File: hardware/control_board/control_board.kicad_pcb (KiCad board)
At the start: 4 copper layers, 70 x 50 mm, 9 parts, among them J1 USB-C, J2 USB-C, J3 TX24-60R-6ST-H1E, J4 TX24-60R-6ST-H1E, U1 STUSB4500QTR

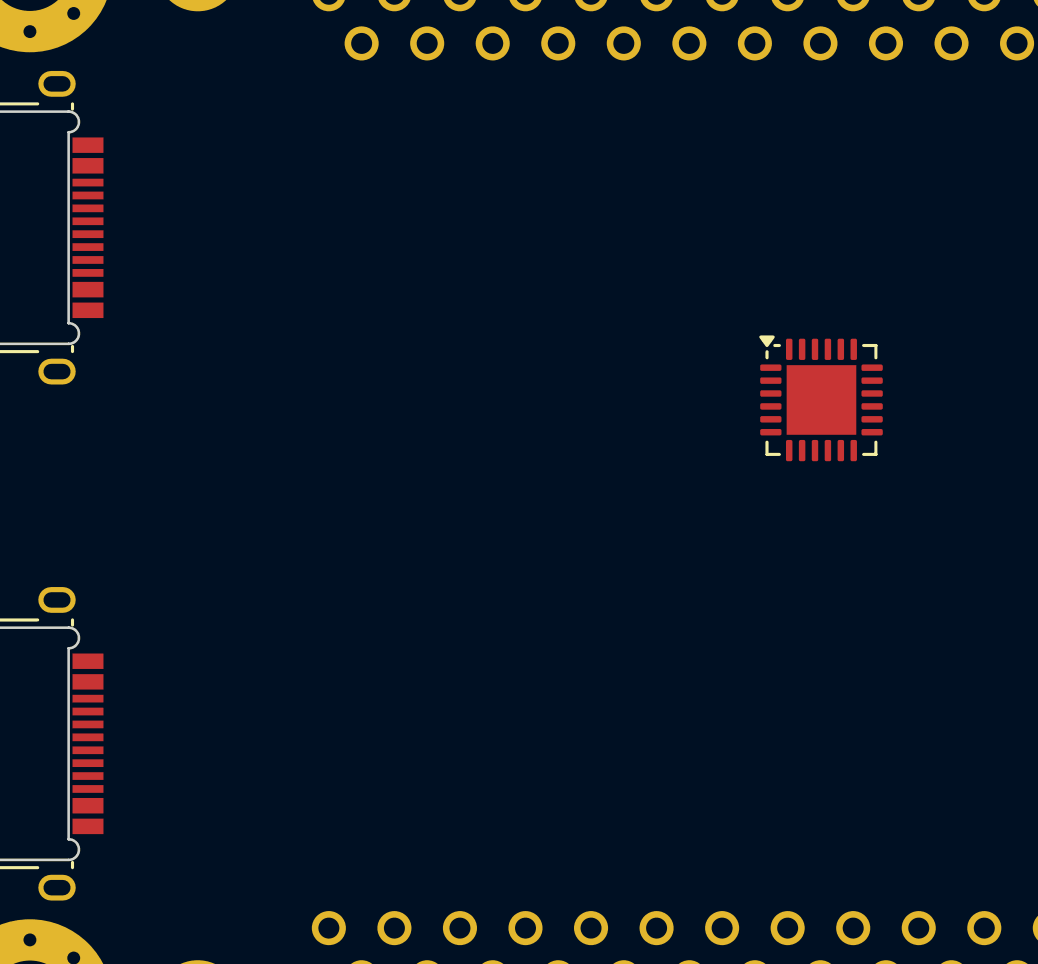
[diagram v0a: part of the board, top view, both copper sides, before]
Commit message: added components to uart bridge
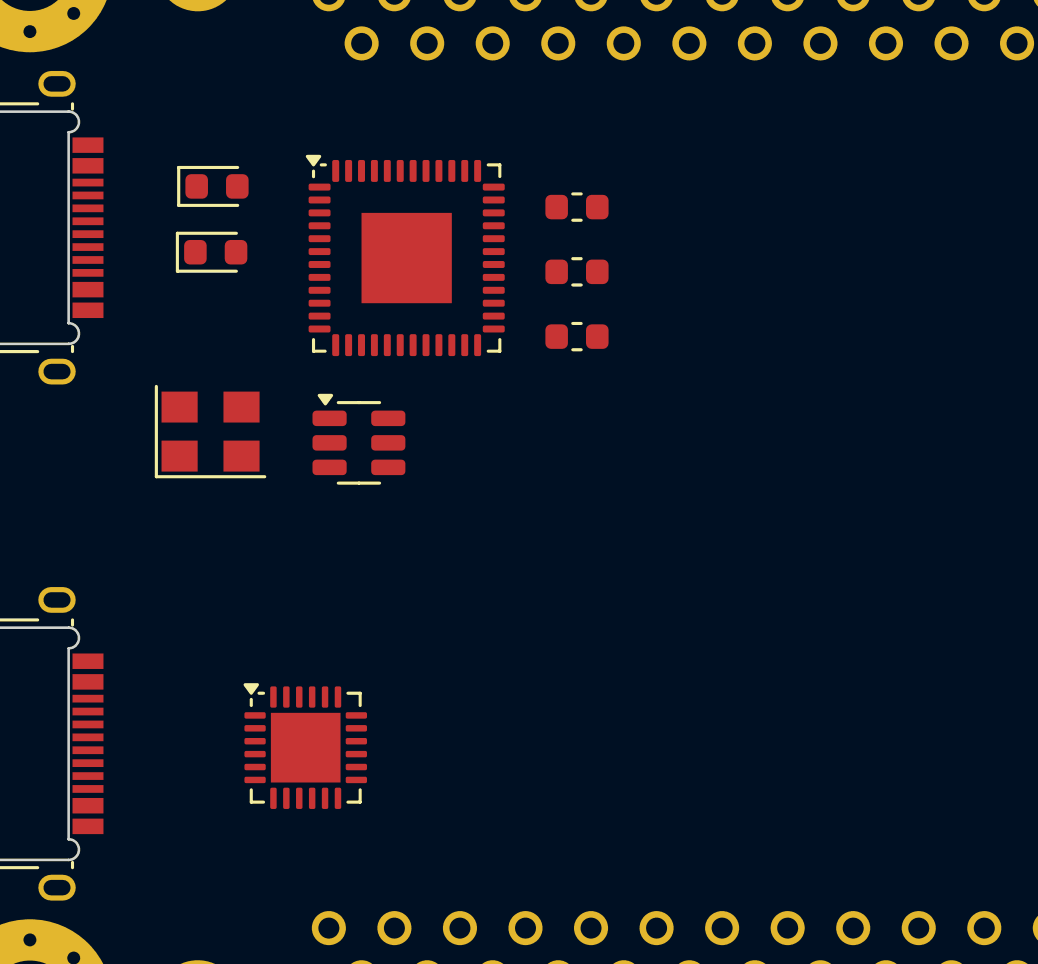
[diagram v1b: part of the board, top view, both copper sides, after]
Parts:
- added D1: PGB1010603MR, Diode_SMD:D_0603_1608Metric, F.Cu at (112.2, 93.4)
- added D2: PGB1010603MR, Diode_SMD:D_0603_1608Metric, F.Cu at (112.2, 96.0)
- added L1: 600ohm/0.5A Core FeSi, Inductor_SMD:L_0603_1608Metric, F.Cu at (126.2, 94.2)
- added L2: 600ohm/0.5A Core FeSi, Inductor_SMD:L_0603_1608Metric, F.Cu at (126.2, 96.7)
- added L3: 600ohm/0.5A Core FeSi, Inductor_SMD:L_0603_1608Metric, F.Cu at (126.2, 99.2)
- added U2: FT232H, Package_DFN_QFN:NXP_LQFN-48-1EP_7x7mm_P0.5mm_EP3.5x3.5mm_16xMask0.45x0.45, F.Cu at (119.6, 96.2)
- added U3: 93LC56BT-I/OT, Package_TO_SOT_SMD:SOT-23-6, F.Cu at (117.8, 103.3)
- added Y1: Crystal_GND24, Crystal:Crystal_SMD_SeikoEpson_FA238V-4Pin_3.2x2.5mm, F.Cu at (112.0, 102.9)
- moved U1 24.1 mm to (115.7, 115.2)
